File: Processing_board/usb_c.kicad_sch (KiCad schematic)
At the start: 20 parts, among them J14 USB4215-03-A_REVA, Q4 DMN66D0LT-7, Q6 DMN66D0LT-7, U16 MCP2200-I_SO

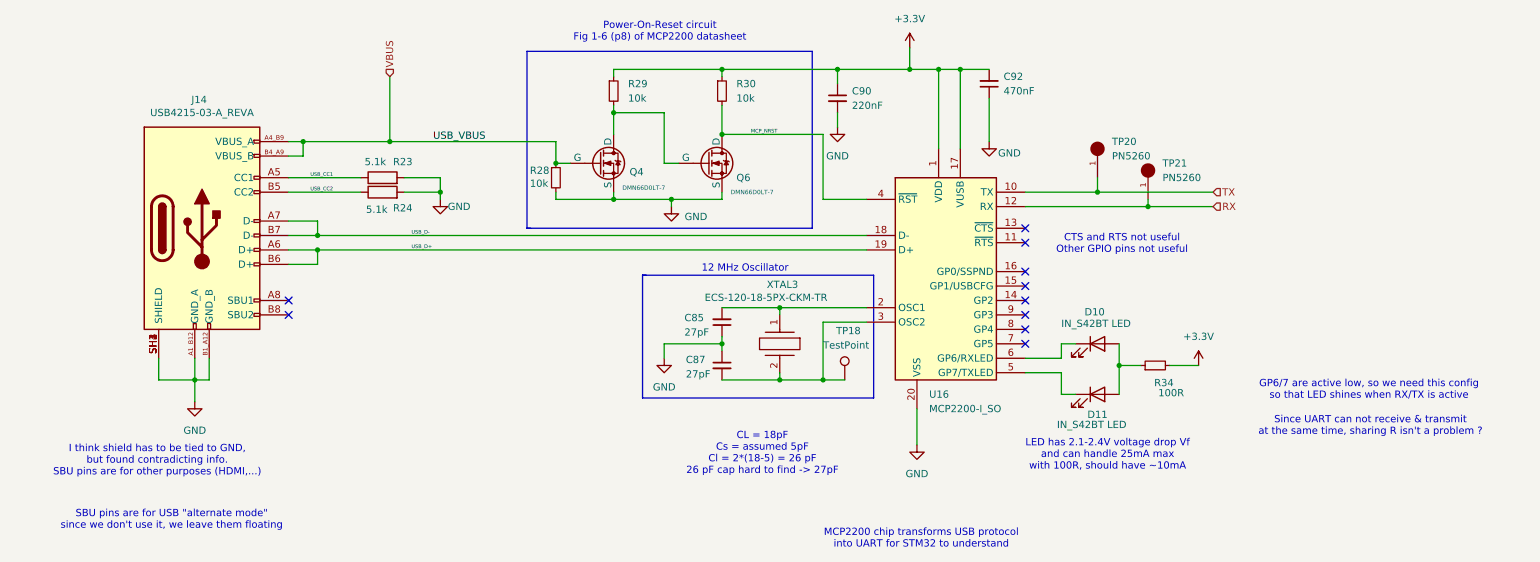
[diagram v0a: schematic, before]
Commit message: had to rename all components on the PCB to match the schematic
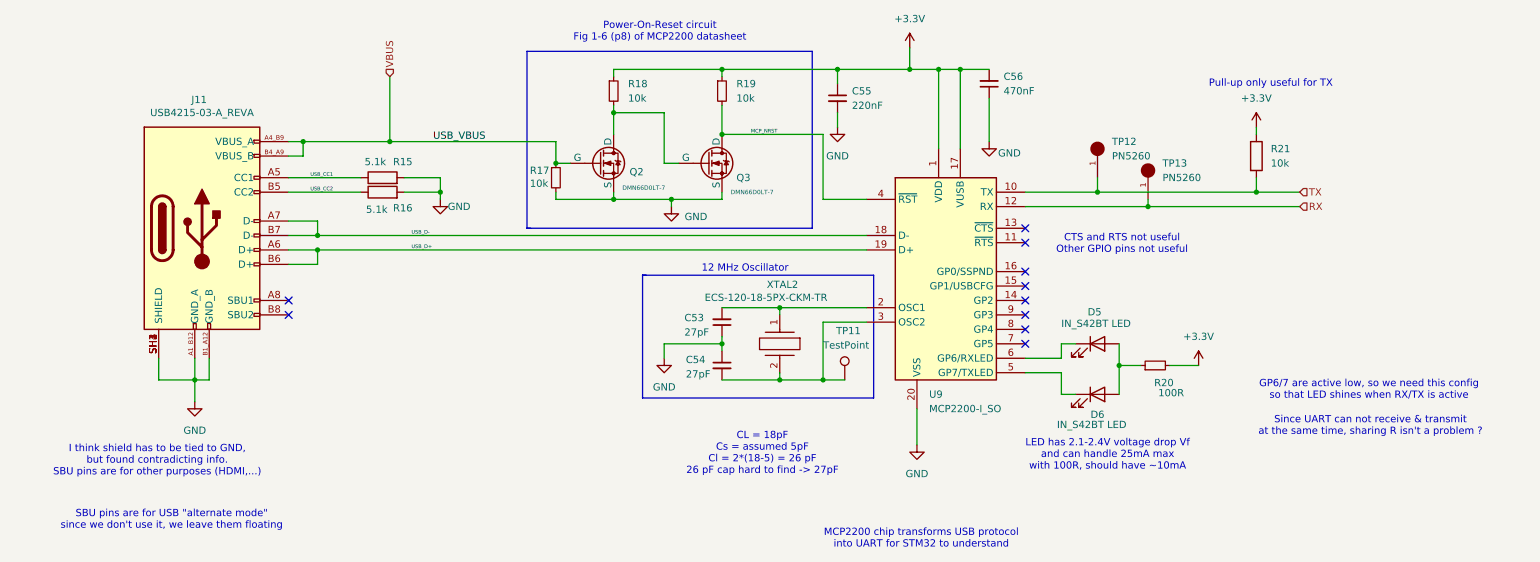
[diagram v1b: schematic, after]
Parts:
- added R21: 10k, Resistor_SMD:R_0402_1005Metric, symbol Device:R
- renumbered C85 to C53, C87 to C54, C90 to C55, C92 to C56, D10 to D5, D11 to D6, J14 to J11, Q4 to Q2, Q6 to Q3, R23 to R15, R24 to R16, R28 to R17, R29 to R18, R30 to R19, R34 to R20, TP18 to TP11, TP20 to TP12, TP21 to TP13, U16 to U9, XTAL3 to XTAL2
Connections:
- net +3.3V: now also R21.1
- net TX: now also R21.2
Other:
- note added: "Pull-up only useful for TX"

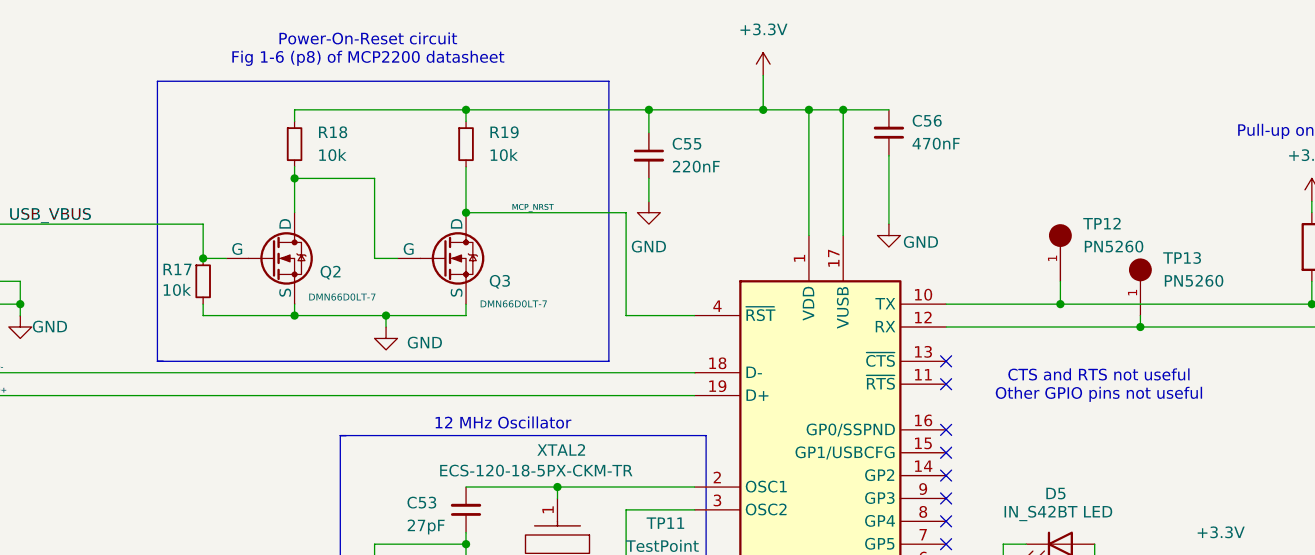
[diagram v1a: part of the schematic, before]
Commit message: created BOM, deleted useless folder Components and renamed CAD_Models to Parts
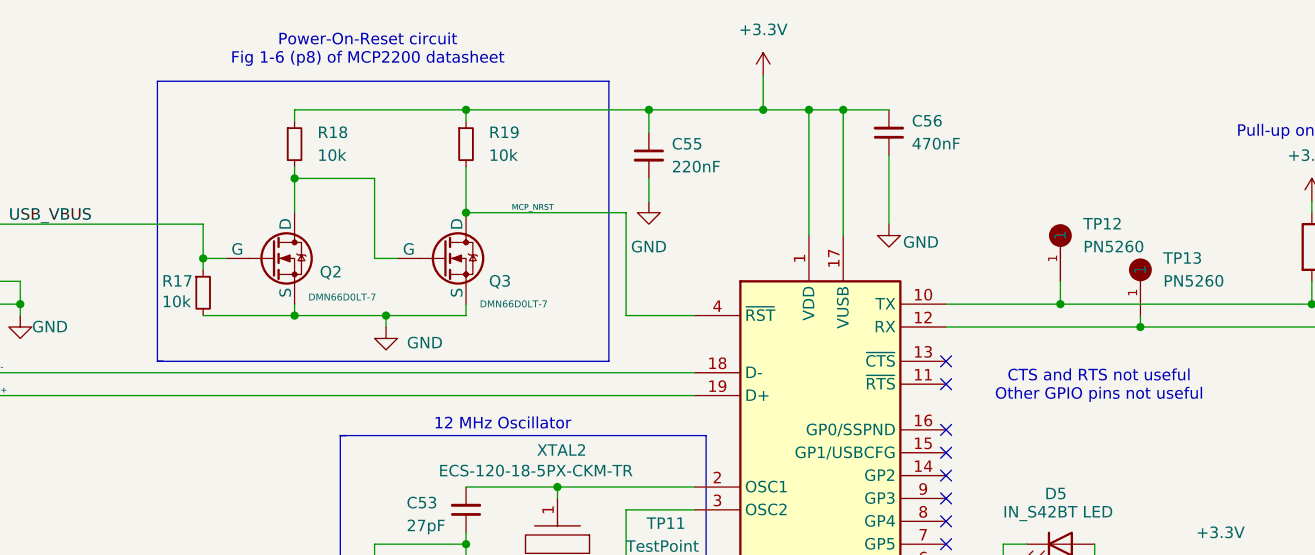
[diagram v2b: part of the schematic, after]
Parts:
- C53, C54: Link (none) -> https://www.mouser.ch/ProductDetail/KYOCERA-AVX/08055C270KA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; MANUFACTURER (none) -> KYOCERA AVX; Manufacturer_Part_Number (none) -> 08055C270KAT2A; Panier (none) -> 1
- C55: Link (none) -> https://www.mouser.ch/ProductDetail/Murata-Electronics/GRT1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; MANUFACTURER (none) -> Murata Electronics; Manufacturer_Part_Number (none) -> GRT155R71A224KE01D; Panier (none) -> 1
- C56: Link (none) -> https://www.mouser.ch/ProductDetail/KEMET/C0402C473K8RACAUT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; MANUFACTURER (none) -> KEMET; Manufacturer_Part_Number (none) -> C0402C473K8RACAUTO7411; Panier (none) -> 1
- D5, D6: Link (none) -> https://www.mouser.ch/ProductDetail/Inolux/IN-S42BT5G?qs=mA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; MANUFACTURER (none) -> Inolux; Manufacturer_Part_Number (none) -> IN-S42BT5G; Panier (none) -> 1
- J11: Link (none) -> https://www.mouser.ch/ProductDetail/GCT/USB4215-03-A?qs=IKk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; MANUFACTURER Global Connector Technology -> CGT; Manufacturer_Part_Number (none) -> USB4215-03-A; déjà (none) -> 1
- Q2, Q3: Link (none) -> https://www.mouser.ch/ProductDetail/Diodes-Incorporated/DMN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; MANUFACTURER (none) -> Diodes Incorporated; Panier (none) -> 1
- R15, R16: Link (none) -> https://www.mouser.ch/ProductDetail/YAGEO/AC0402JR-075K1L?q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; MANUFACTURER (none) -> YAGEO; Manufacturer_Part_Number (none) -> AC0402JR-075K1L; Panier (none) -> 1
- R17, R18, R19, R21: Link (none) -> https://www.mouser.ch/ProductDetail/Wurth-Elektronik/560112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; MANUFACTURER (none) -> Wurth Elektronik; Manufacturer_Part_Number (none) -> 560112110020; Panier (none) -> 1
- R20: Link (none) -> https://www.mouser.ch/ProductDetail/KOA-Speer/RK73B1ETTPD10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; MANUFACTURER (none) -> KOA Speer; Manufacturer_Part_Number (none) -> RK73B1ETTPD101J; Panier (none) -> 1
- TP12, TP13: Link (none) -> https://www.mouser.ch/ProductDetail/Keystone-Electronics/52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; Manufacturer_Part_Number (none) -> 5260; Panier (none) -> 1
- U9: Link (none) -> https://www.mouser.ch/ProductDetail/Microchip-Technology/MC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; MANUFACTURER (none) -> Microchip Technology; Panier (none) -> 1
- XTAL2: Link (none) -> https://www.mouser.ch/ProductDetail/ECS/ECS-120-18-5PX-CKM-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; MANUFACTURER (none) -> ECS; Panier (none) -> 1
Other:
- moved on the sheet: R17

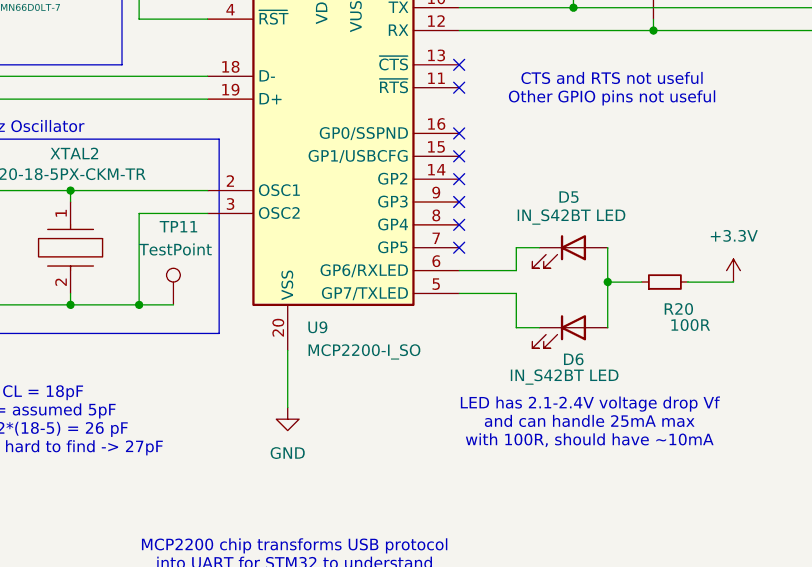
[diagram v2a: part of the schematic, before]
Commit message: correct text height/width for silkscreen, correct 3D models for THT pin headers
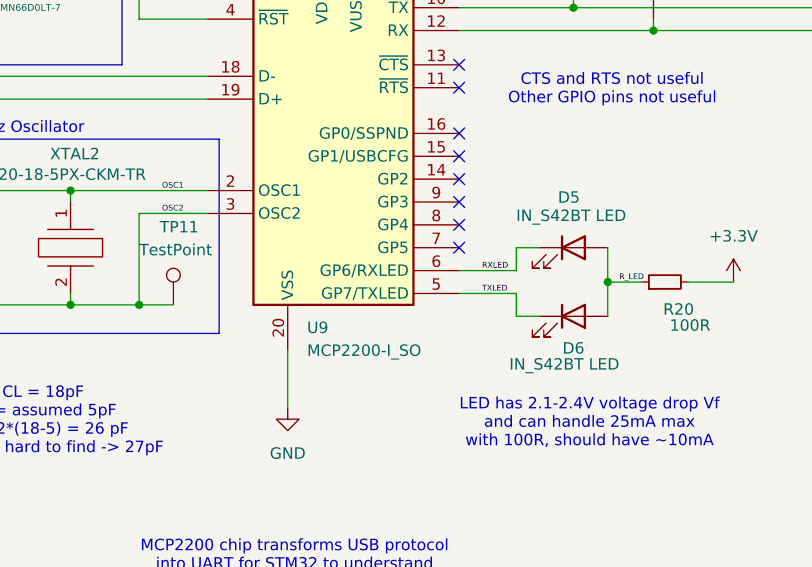
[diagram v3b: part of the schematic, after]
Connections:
- net OSC1: now reaches C53.2, U9.2 (OSC1), XTAL2.1
- net OSC2: now reaches C54.2, TP11.1, U9.3 (OSC2), XTAL2.2
- net TXLED: now reaches D6.1 (K), U9.5 (GP7/TXLED)
- net RXLED: now reaches D5.1 (K), U9.6 (GP6/RXLED)
- net R_LED: now reaches D5.2 (A), D6.2 (A), R20.1
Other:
- moved on the sheet: D6
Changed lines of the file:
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@@
 	(wire
 		(pts
-			(xy 212.09 101.6) (xy 208.28 101.6)
+			(xy 208.28 101.6) (xy 212.09 101.6)
 		)
 		(stroke
@@
 	(wire
 		(pts
-			(xy 198.12 106.68) (xy 200.66 106.68)
-		)
-		(stroke
-			(width 0)
-			(type default)
-		)
-	)
-	(wire
-		(pts
-			(xy 198.12 106.68) (xy 198.12 102.87)
+			(xy 198.12 105.41) (xy 200.66 105.41)
+		)
+		(stroke
+			(width 0)
+			(type default)
+		)
+	)
+	(wire
+		(pts
+			(xy 198.12 105.41) (xy 198.12 102.87)
 		)
 		(stroke
@@
 	(wire
 		(pts
-			(xy 208.28 101.6) (xy 208.28 106.68)
+			(xy 208.28 101.6) (xy 208.28 105.41)
 		)
 		(stroke
@@
 			(width 0)
 			(type default)
+		)
+	)
+	(label "OSC1"
+		(at 158.75 91.44 0)
+		(effects
+			(font
+				(size 0.635 0.635)
+			)
+			(justify left bottom)
 		)
 	)
@@
 		)
 	)
+	(label "R_LED"
+		(at 209.55 101.6 0)
+		(effects
+			(font
+				(size 0.635 0.635)
+			)
+			(justify left bottom)
+		)
+	)
 	(label "USB_CC1"
 		(at 66.04 68.58 0)
@@
 		)
 	)
+	(label "OSC2"
+		(at 158.75 93.98 0)
+		(effects
+			(font
+				(size 0.635 0.635)
+			)
+			(justify left bottom)
+		)
+	)
 	(label "USB_D+"
 		(at 83.82 81.28 0)
+		(effects
+			(font
+				(size 0.635 0.635)
+			)
+			(justify left bottom)
+		)
+	)
+	(label "TXLED"
+		(at 194.31 102.87 0)
+		(effects
+			(font
+				(size 0.635 0.635)
+			)
+			(justify left bottom)
+		)
+	)
+	(label "RXLED"
+		(at 194.31 100.33 0)
 		(effects
 			(font
@@
 	(symbol
 		(lib_id "Device:LED")
-		(at 204.47 106.68 0)
+		(at 204.47 105.41 0)
 		(unit 1)
 		(exclude_from_sim no)
@@
 		(dnp no)
 		(property "Reference" "D6"
-			(at 204.47 110.236 0)
+			(at 204.47 108.966 0)
 			(effects
 				(font
@@
 		)
 		(property "Value" "IN_S42BT LED"
-			(at 203.454 112.014 0)
+			(at 203.454 110.744 0)
 			(effects
 				(font
@@
 		)
 		(property "Footprint" "LED_SMD:LED_0402_1005Metric"
-			(at 204.47 106.68 0)
+			(at 204.47 105.41 0)
 			(effects
 				(font
@@
 		)
 		(property "Datasheet" "~"
-			(at 204.47 106.68 0)
+			(at 204.47 105.41 0)
 			(effects
 				(font
@@
 		)
 		(property "Description" "Light emitting diode"
-			(at 204.47 106.68 0)
+			(at 204.47 105.41 0)
 			(effects
 				(font
@@
 		)
 		(property "Sim.Pins" "1=K 2=A"
-			(at 204.47 106.68 0)
+			(at 204.47 105.41 0)
 			(effects
 				(font
@@
 		)
 		(property "Link" "https://www.mouser.ch/ProductDetail/Inolux/IN-S42BT5G?qs=mAH9sUMRCttW6d2tLN392Q%3D%3D"
-			(at 204.47 106.68 0)
+			(at 204.47 105.41 0)
 			(effects
 				(font
@@
 		)
 		(property "Panier" "1"
-			(at 204.47 106.68 0)
+			(at 204.47 105.41 0)
 			(effects
 				(font
@@
 		)
 		(property "MANUFACTURER" "Inolux"
-			(at 204.47 106.68 0)
+			(at 204.47 105.41 0)
 			(effects
 				(font
@@
 		)
 		(property "Manufacturer_Part_Number" "IN-S42BT5G "
-			(at 204.47 106.68 0)
+			(at 204.47 105.41 0)
 			(effects
 				(font
@@
 		)
 		(property "déjà" ""
-			(at 204.47 106.68 0)
-			(effects
-				(font
+			(at 204.47 105.41 0)
+			(effects
+				(font
